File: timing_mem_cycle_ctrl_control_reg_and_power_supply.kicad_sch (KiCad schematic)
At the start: 55 parts, among them U10 LS175, U11 LS20, U19 LS04, U20 LS10, U21 LS161, U30 LS20, U31 LS00, U32 LS109, U4 LS04, U42 LS109, U5 LS109, U50 LS368, U51 LS04, U52 LS00, U53 LS04, U57 LS13, U60 7406, U62 LS08

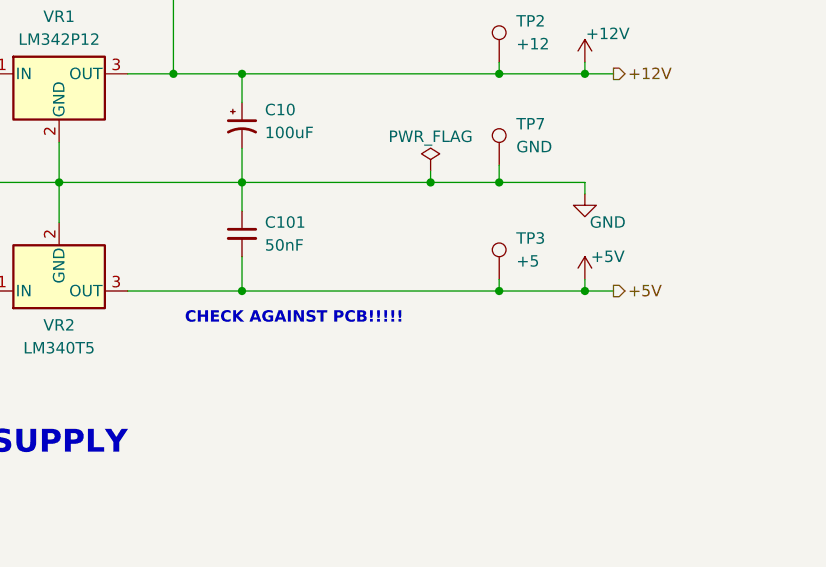
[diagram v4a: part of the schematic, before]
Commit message: Completed first version of board routing
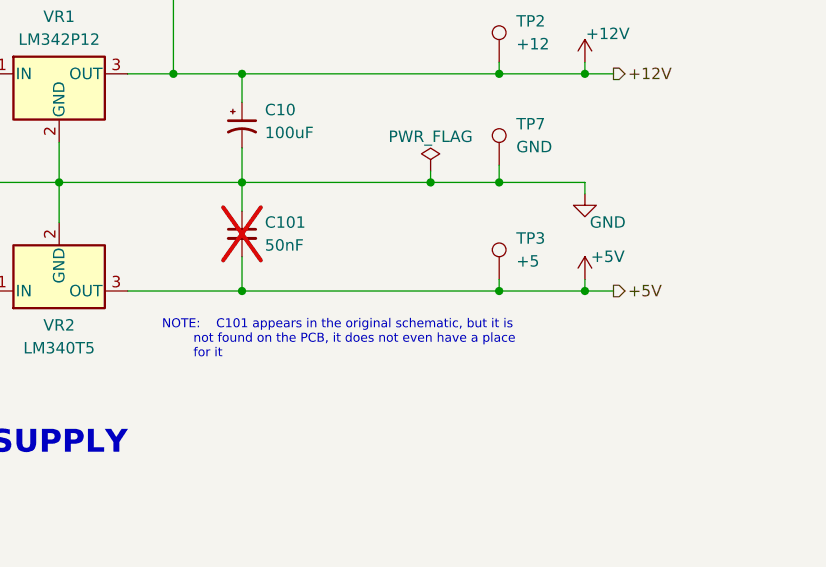
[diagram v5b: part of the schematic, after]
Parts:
- C101: now not fitted
- R13, R14, R5: footprint K_1013:R_Axial_DIN0204_L3.6mm_D2.5mm_P12.70mm_Horizontal -> K_1013:R_Axial_DIN0204_L3.6mm_D2.5mm_P12.70mm_Horizontal_10K
- R22: footprint K_1013:R_Axial_DIN0309_L9.0mm_D3.2mm_P12.70mm_Horizontal -> K_1013:R_Axial_DIN0204_L3.6mm_D2.5mm_P12.70mm_Horizontal_10K
- R28, R31, R53: footprint K_1013:R_Axial_DIN0309_L9.0mm_D3.2mm_P12.70mm_Horizontal -> K_1013:R_Axial_DIN0204_L3.6mm_D2.5mm_P12.70mm_Horizontal_470R
- R29: footprint K_1013:R_Axial_DIN0309_L9.0mm_D3.2mm_P12.70mm_Horizontal -> K_1013:R_Axial_DIN0204_L3.6mm_D2.5mm_P12.70mm_Horizontal_10R
- R30, R54: footprint K_1013:R_Axial_DIN0309_L9.0mm_D3.2mm_P12.70mm_Horizontal -> K_1013:R_Axial_DIN0204_L3.6mm_D2.5mm_P12.70mm_Horizontal_2K2
- R55: footprint K_1013:R_Axial_DIN0309_L9.0mm_D3.2mm_P12.70mm_Horizontal -> K_1013:R_Axial_DIN0204_L3.6mm_D2.5mm_P12.70mm_Horizontal_3K3
- R6: footprint K_1013:R_Axial_DIN0204_L3.6mm_D2.5mm_P12.70mm_Horizontal -> K_1013:R_Axial_DIN0204_L3.6mm_D2.5mm_P12.70mm_Horizontal_1K
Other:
- note added: "NOTE: C101 appears in the original schematic, but it is not found on the PCB, it does not even have a place for it"
- note removed: "CHECK AGAINST PCB!!!!!"
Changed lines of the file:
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@@
     (stroke (width 0) (type default))
-  )
-  (text "CHECK AGAINST PCB!!!!!" (at 335.28 226.06 0)
-    (effects (font (size 1.27 1.27) (thickness 0.254) bold (color 194 0 0 1)) (justify left bottom))
   )
   (text "POWER SUPPLY\n" (at 328.93 240.665 0)
@@
   (text "CLOCK" (at 125.095 213.36 0)
     (effects (font (size 1.27 1.27)) (justify left bottom))
+  )
+  (text "NOTE:	C101 appears in the original schematic, but it is\n		not found on the PCB, it does not even have a place\n		for it"
+    (at 332.74 229.87 0)
+    (effects (font (size 1 1) (color 194 0 0 1)) (justify left bottom))
   )
   (label "RAS" (at 187.96 120.015 0) (fields_autoplaced)
@@
       (effects (font (size 1.27 1.27)))
     )
-    (property "Footprint" "K_1013:R_Axial_DIN0309_L9.0mm_D3.2mm_P12.70mm_Horizontal" (at 266.7 254.635 0)
+    (property "Footprint" "K_1013:R_Axial_DIN0204_L3.6mm_D2.5mm_P12.70mm_Horizontal_10K" (at 266.7 254.635 0)
       (effects (font (size 1.27 1.27)) hide)
     )
@@
       (effects (font (size 1.27 1.27)))
     )
-    (property "Footprint" "K_1013:R_Axial_DIN0204_L3.6mm_D2.5mm_P12.70mm_Horizontal" (at 334.01 173.99 0)
+    (property "Footprint" "K_1013:R_Axial_DIN0204_L3.6mm_D2.5mm_P12.70mm_Horizontal_1K" (at 334.01 173.99 0)
       (effects (font (size 1.27 1.27)) hide)
     )
@@
       (effects (font (size 1.27 1.27)))
     )
-    (property "Footprint" "K_1013:R_Axial_DIN0204_L3.6mm_D2.5mm_P12.70mm_Horizontal" (at 127 57.785 0)
+    (property "Footprint" "K_1013:R_Axial_DIN0204_L3.6mm_D2.5mm_P12.70mm_Horizontal_10K" (at 127 57.785 0)
       (effects (font (size 1.27 1.27)) hide)
     )
@@
       (effects (font (size 1.27 1.27)))
     )
-    (property "Footprint" "K_1013:R_Axial_DIN0309_L9.0mm_D3.2mm_P12.70mm_Horizontal" (at 92.71 213.995 0)
+    (property "Footprint" "K_1013:R_Axial_DIN0204_L3.6mm_D2.5mm_P12.70mm_Horizontal_10R" (at 92.71 213.995 0)
       (effects (font (size 1.27 1.27)) hide)
     )
@@
       (effects (font (size 1.27 1.27)))
     )
-    (property "Footprint" "K_1013:R_Axial_DIN0309_L9.0mm_D3.2mm_P12.70mm_Horizontal" (at 86.995 200.025 0)
+    (property "Footprint" "K_1013:R_Axial_DIN0204_L3.6mm_D2.5mm_P12.70mm_Horizontal_470R" (at 86.995 200.025 0)
       (effects (font (size 1.27 1.27)) hide)
     )
@@
       (effects (font (size 1.27 1.27)))
     )
-    (property "Footprint" "K_1013:R_Axial_DIN0309_L9.0mm_D3.2mm_P12.70mm_Horizontal" (at 113.665 207.645 0)
+    (property "Footprint" "K_1013:R_Axial_DIN0204_L3.6mm_D2.5mm_P12.70mm_Horizontal_470R" (at 113.665 207.645 0)
       (effects (font (size 1.27 1.27)) hide)
     )
@@
       (effects (font (size 1.27 1.27)))
     )
-    (property "Footprint" "K_1013:R_Axial_DIN0309_L9.0mm_D3.2mm_P12.70mm_Horizontal" (at 114.935 96.52 0)
+    (property "Footprint" "K_1013:R_Axial_DIN0204_L3.6mm_D2.5mm_P12.70mm_Horizontal_2K2" (at 114.935 96.52 0)
       (effects (font (size 1.27 1.27)) hide)
     )
@@
   )
   (symbol (lib_id "Device:C_Small") (at 341.63 215.9 0) (unit 1)
-    (in_bom yes) (on_board yes) (dnp no) (fields_autoplaced)
+    (in_bom yes) (on_board no) (dnp yes) (fields_autoplaced)
     (property "Reference" "C101" (at 344.17 214.6363 0)
       (effects (font (size 1.27 1.27)) (justify left))
@@
       (effects (font (size 1.27 1.27)) (justify left))
     )
-    (property "Footprint" "K_1013:R_Axial_DIN0309_L9.0mm_D3.2mm_P12.70mm_Horizontal" (at 348.615 55.245 0)
+    (property "Footprint" "K_1013:R_Axial_DIN0204_L3.6mm_D2.5mm_P12.70mm_Horizontal_470R" (at 348.615 55.245 0)
       (effects (font (size 1.27 1.27)) hide)
     )
@@
       (effects (font (size 1.27 1.27)))
     )
-    (property "Footprint" "K_1013:R_Axial_DIN0309_L9.0mm_D3.2mm_P12.70mm_Horizontal" (at 114.935 100.33 0)
+    (property "Footprint" "K_1013:R_Axial_DIN0204_L3.6mm_D2.5mm_P12.70mm_Horizontal_3K3" (at 114.935 100.33 0)
       (effects (font (size 1.27 1.27)) hide)
     )
@@
       (effects (font (size 1.27 1.27)))
     )
-    (property "Footprint" "K_1013:R_Axial_DIN0204_L3.6mm_D2.5mm_P12.70mm_Horizontal" (at 238.76 254.635 0)
+    (property "Footprint" "K_1013:R_Axial_DIN0204_L3.6mm_D2.5mm_P12.70mm_Horizontal_10K" (at 238.76 254.635 0)
       (effects (font (size 1.27 1.27)) hide)
     )
@@
       (effects (font (size 1.27 1.27)))
     )
-    (property "Footprint" "K_1013:R_Axial_DIN0204_L3.6mm_D2.5mm_P12.70mm_Horizontal" (at 252.73 254.635 0)
+    (property "Footprint" "K_1013:R_Axial_DIN0204_L3.6mm_D2.5mm_P12.70mm_Horizontal_10K" (at 252.73 254.635 0)
       (effects (font (size 1.27 1.27)) hide)
     )
@@
       (effects (font (size 1.27 1.27)))
     )
-    (property "Footprint" "K_1013:R_Axial_DIN0309_L9.0mm_D3.2mm_P12.70mm_Horizontal" (at 98.425 200.025 0)
-      (effects (font (size 1.27 1.27)) hide)
-    )
+    (property "Footprint" "K_1013:R_Axial_DIN0204_L3.6mm_D2.5mm_P12.70mm_Horizontal_2K2" (at 98.425 200.025 0)
+      (effects (font (size 1.27 1.27)) hide)
+    )

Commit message: Cosmetic changes
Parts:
- U30: symbol 74xx:74LS20 -> LS_Logic:74LS20_U30
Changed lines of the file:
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@@
     (pin "1")
     (pin "6")
+    (pin "11")
+    (pin "3")
     (instances
       (project "k-1013-floppy-controller-replica"
@@
     )
   )
-  (symbol (lib_id "74xx:74LS20") (at 316.865 104.14 0) (unit 1)
+  (symbol (lib_id "LS_Logic:74LS20_U30") (at 316.865 104.14 0) (unit 1)
     (in_bom yes) (on_board yes) (dnp no)
     (property "Reference" "U30" (at 316.865 102.87 0)
@@
     (pin "7")
     (pin "2")
+    (pin "3")
+    (pin "11")
     (instances
       (project "k-1013-floppy-controller-replica"
@@
     (pin "1")
     (pin "6")
-    (instances
-      (project "k-1013-floppy-controller-replica"
+    (pin "11")
+    (pin "3")
+    (instances
+      (project "k-1013-floppy-controller-replica"
